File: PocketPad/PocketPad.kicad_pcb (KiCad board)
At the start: 2 copper layers, 71.6 x 60.5 mm, 35 parts, among them SW0 SW_Push, SW1 SW_Push, SW10 SW_Push, SW11 SW_Push, SW12 SW_Push, SW13 SW_Push, SW14 SW_Push, SW15 SW_Push, SW16 SW_Push, SW2 SW_Push, SW3 SW_Push, SW4 SW_Push, SW5 SW_Push, SW6 SW_Push, SW7 SW_Push, SW8 SW_Push, SW9 SW_Push

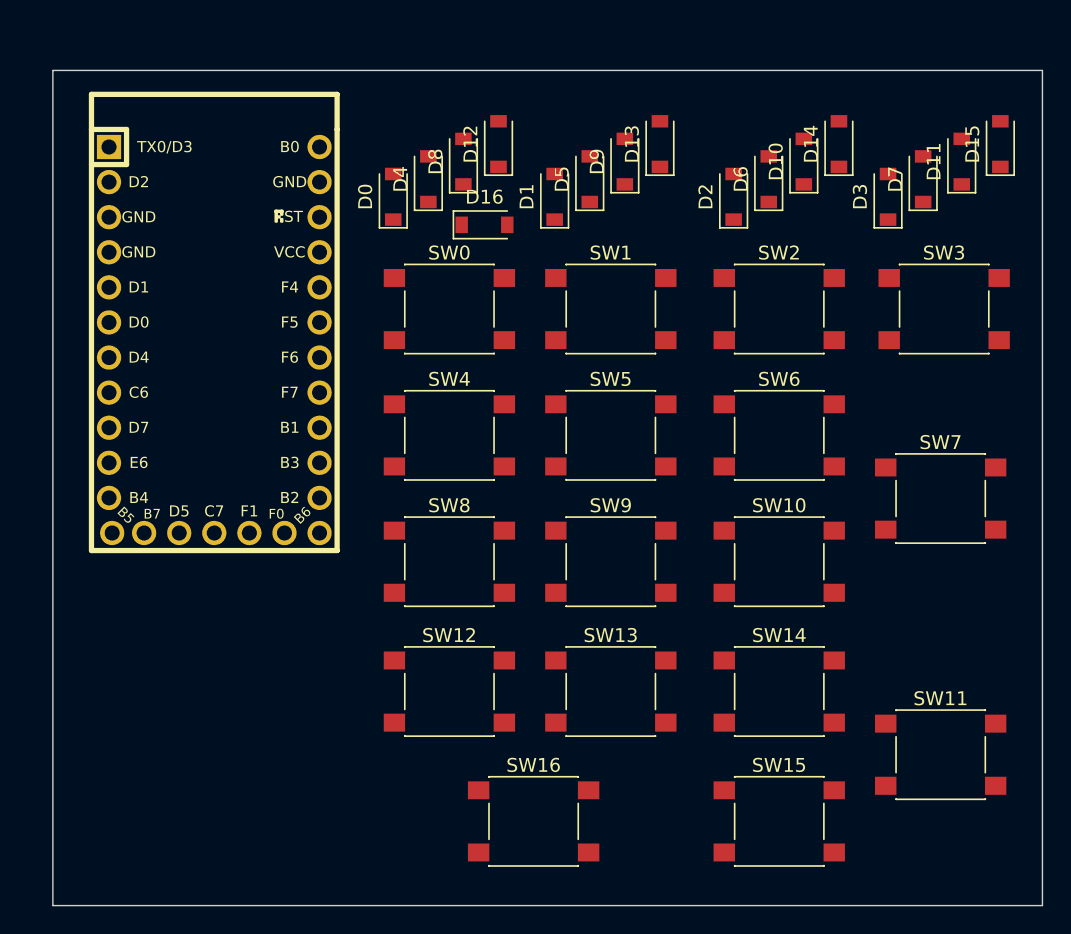
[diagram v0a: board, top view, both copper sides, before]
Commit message: Replaced Diodes. Added 3D models
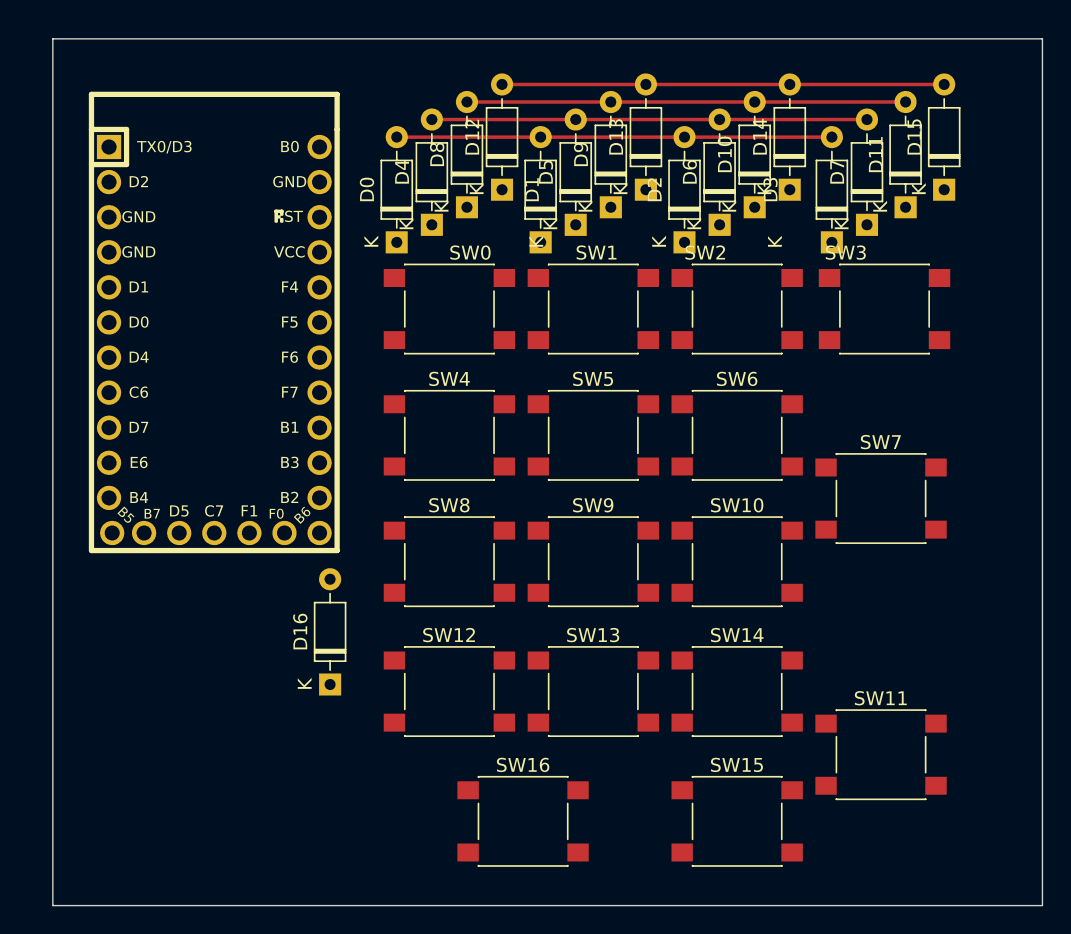
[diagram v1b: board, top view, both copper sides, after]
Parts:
- D0, D1, D10, D11, D12, D13, D14, D15, D16, D2, D3, D4, D5, D6, D7, D8, D9: footprint Diode_SMD:D_SOD-123 -> Diode_THT:D_DO-35_SOD27_P7.62mm_Horizontal
- moved D16 35.1 mm to (45.7, 82.5), turned to 90 degrees
- moved D7 5.24 mm to (84.6, 49.3)
- moved D11 5.24 mm to (87.4, 48.0)
- moved D15 5.24 mm to (90.2, 46.7)
- moved D3 5.24 mm to (82.0, 50.5)
- moved D10 4.85 mm to (76.5, 48.0)
- moved D2 4.85 mm to (71.4, 50.5)
- moved D6 4.85 mm to (73.9, 49.3)
- moved D14 4.85 mm to (79.0, 46.7)
- moved SW11 4.32 mm to (85.6, 87.6)
- moved SW3 4.32 mm to (85.9, 55.4)
- moved SW7 4.32 mm to (85.6, 69.1)
- moved D5 3.45 mm to (63.5, 49.3)
- moved D13 3.45 mm to (68.6, 46.7)
- moved D1 3.45 mm to (61.0, 50.5)
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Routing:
- net ROW3: track 0.00 -> 32.0 mm
- net ROW2: track 0.00 -> 31.8 mm
- net ROW0: track 0.00 -> 31.5 mm
- net ROW1: track 0.00 -> 31.5 mm
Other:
- board size 71.6 x 60.5 mm -> 71.6 x 62.7 mm

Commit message: V0.1 Complete
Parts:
- added D17: DIODE, Diode_THT:D_DO-35_SOD27_P7.62mm_Horizontal, F.Cu at (42.2, 82.5)
- added D18: DIODE, Diode_THT:D_DO-35_SOD27_P7.62mm_Horizontal, F.Cu at (46.5, 82.5)
- added SW17: SW_Push, Keebio:Switch_6x6x8.5, F.Cu at (44.7, 92.5)
- added SW18: SW_Push, Keebio:Switch_6x6x8.5, F.Cu at (59.9, 92.5)
- SW0, SW1, SW10, SW11, SW12, SW13, SW14, SW15, SW16, SW2, SW3, SW4, SW5, SW6, SW7, SW8, SW9: footprint Button_Switch_SMD:SW_SPST_PTS645 -> Keebio:Switch_6x6x8.5
- moved SW16 26.4 mm to (33.3, 92.5)
- moved D3 11.7 mm to (93.0, 46.2)
- moved D2 11.0 mm to (81.5, 46.2)
- moved D1 10.1 mm to (70.1, 46.2)
- moved D0 9.20 mm to (58.7, 46.2)
- moved D12 8.54 mm to (50.3, 50.0)
- moved D16 8.38 mm to (37.3, 82.5)
- moved D13 7.61 mm to (61.7, 50.0)
- moved D14 6.71 mm to (73.2, 50.0)
- moved D15 6.49 mm to (84.6, 50.0)
- moved D7 5.86 mm to (90.2, 47.5)
- moved D6 5.14 mm to (78.7, 47.5)
- moved D5 4.20 mm to (67.3, 47.5)
- moved D4 3.31 mm to (55.9, 47.5)
- moved D8 2.65 mm to (53.1, 48.8)
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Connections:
- D16 pad 2: unconnected-(D16-Pad2) -> ROW4
- MCU1 pad 16: unconnected-(MCU1-Pad16) -> ROW4
- MCU1 pad 17: unconnected-(MCU1-Pad17) -> ROW0
- MCU1 pad 18: unconnected-(MCU1-Pad18) -> ROW1
- MCU1 pad 19: unconnected-(MCU1-Pad19) -> ROW2
- MCU1 pad 20: unconnected-(MCU1-Pad20) -> ROW3
- MCU1 pad 25: unconnected-(MCU1-Pad25) -> COL0
- MCU1 pad 26: unconnected-(MCU1-Pad26) -> COL1
- MCU1 pad 27: unconnected-(MCU1-Pad27) -> COL2
- MCU1 pad 28: unconnected-(MCU1-Pad28) -> COL3
- SW0 pad 1: Net-(SW0-Pad1) -> COL0
- SW1 pad 1: Net-(SW1-Pad1) -> COL1
- SW10 pad 1: Net-(SW10-Pad1) -> COL2
- SW11 pad 1: Net-(SW11-Pad1) -> COL3
- SW12 pad 1: Net-(SW0-Pad1) -> COL0
- SW13 pad 1: Net-(SW1-Pad1) -> COL1
- SW14 pad 1: Net-(SW10-Pad1) -> COL2
- SW15 pad 1: Net-(SW11-Pad1) -> COL3
- SW16 pad 1: Net-(SW0-Pad1) -> COL0
- SW2 pad 1: Net-(SW10-Pad1) -> COL2
- SW3 pad 1: Net-(SW11-Pad1) -> COL3
- SW4 pad 1: Net-(SW0-Pad1) -> COL0
- SW5 pad 1: Net-(SW1-Pad1) -> COL1
- SW6 pad 1: Net-(SW10-Pad1) -> COL2
- SW7 pad 1: Net-(SW11-Pad1) -> COL3
- SW8 pad 1: Net-(SW0-Pad1) -> COL0
- SW9 pad 1: Net-(SW1-Pad1) -> COL1
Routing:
- net COL3: track 0.00 -> 137.9 mm
- net COL2: track 0.00 -> 118.6 mm
- net COL1: track 0.00 -> 99.5 mm
- net COL0: track 0.00 -> 68.4 mm
- net Net-(D15-Pad1): track 0.00 -> 49.0 mm
- net Net-(D11-Pad1): track 0.00 -> 38.4 mm
- net Net-(D13-Pad1): track 0.00 -> 34.8 mm
- net Net-(D12-Pad1): track 0.00 -> 34.0 mm
- net Net-(D14-Pad1): track 0.00 -> 33.8 mm
- net ROW0: track 31.5 -> 64.7 mm
- net ROW1: track 31.5 -> 58.8 mm
- net Net-(D8-Pad1): track 0.00 -> 24.7 mm
- net Net-(D9-Pad1): track 0.00 -> 24.7 mm
- net Net-(D10-Pad1): track 0.00 -> 24.6 mm
- net Net-(D18-Pad1): track 0.00 -> 23.5 mm, vias 0 -> 1
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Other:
- board outline removed

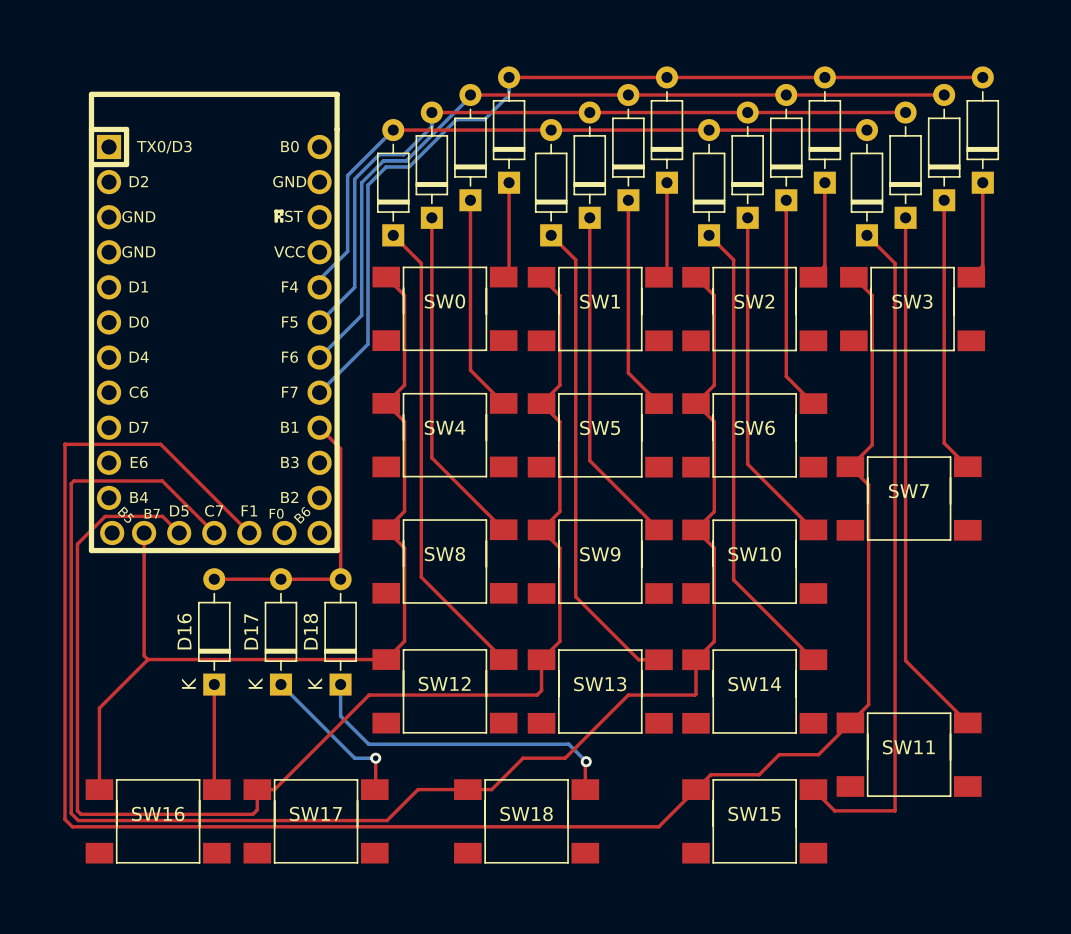
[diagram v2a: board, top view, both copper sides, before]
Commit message: Added GND plane
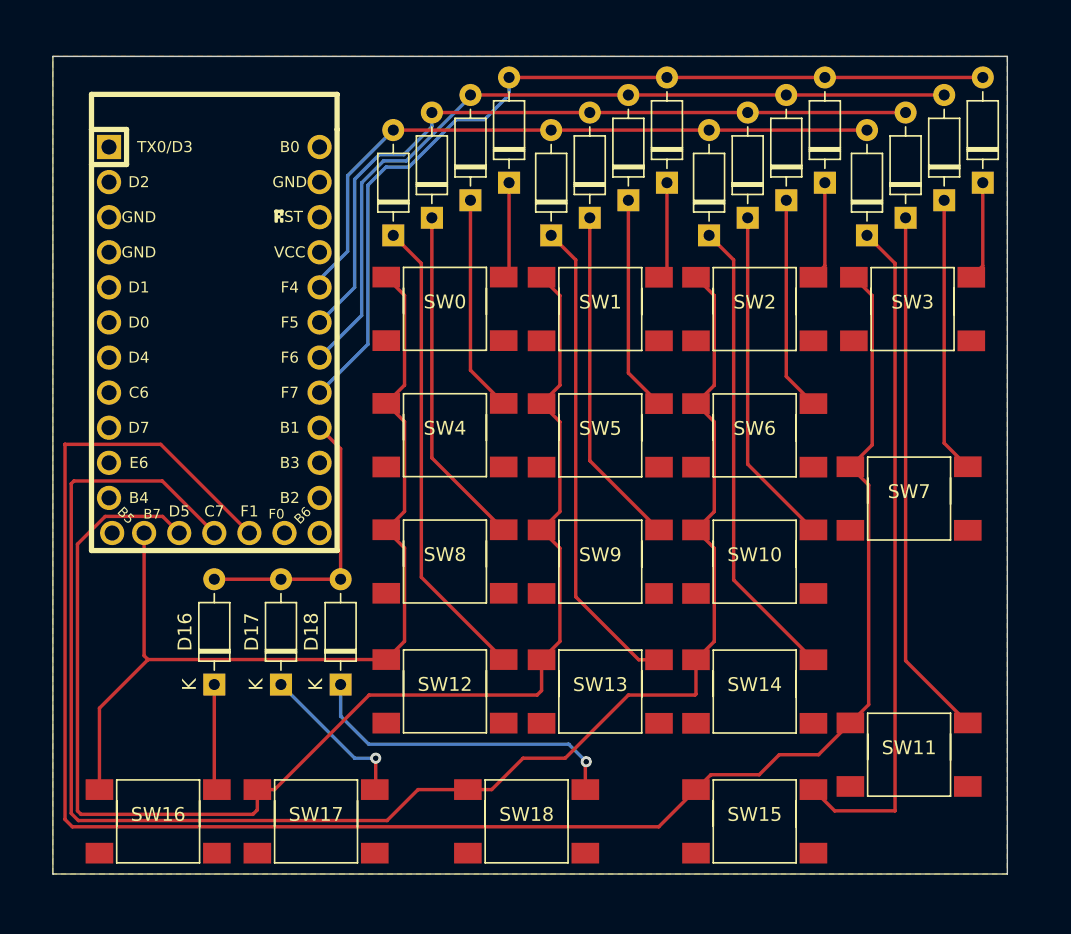
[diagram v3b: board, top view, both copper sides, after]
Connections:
- MCU1 pad 3: unconnected-(MCU1-Pad3) -> GND
- MCU1 pad 4: unconnected-(MCU1-Pad4) -> GND
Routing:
- added copper zone on F.Cu, net GND
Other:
- board outline added: 69.1 x 59.2 mm
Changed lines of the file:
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@@
   (net 1 "unconnected-(MCU1-Pad1)")
   (net 2 "unconnected-(MCU1-Pad2)")
-  (net 3 "unconnected-(MCU1-Pad3)")
-  (net 4 "unconnected-(MCU1-Pad4)")
+  (net 3 "Net-(D17-Pad1)")
+  (net 4 "GND")
   (net 5 "unconnected-(MCU1-Pad5)")
   (net 6 "unconnected-(MCU1-Pad6)")
@@
   (net 42 "ROW4")
   (net 43 "Net-(D16-Pad1)")
-  (net 44 "Net-(SW17-Pad2)")
-  (net 45 "Net-(D18-Pad1)")
-  (net 46 "unconnected-(MCU1-Pad13)")
-  (net 47 "unconnected-(MCU1-Pad14)")
-  (net 48 "unconnected-(MCU1-Pad15)")
+  (net 44 "Net-(D18-Pad1)")
+  (net 45 "unconnected-(MCU1-Pad13)")
+  (net 46 "unconnected-(MCU1-Pad14)")
+  (net 47 "unconnected-(MCU1-Pad15)")
   (footprint "Diode_THT:D_DO-35_SOD27_P7.62mm_Horizontal" (layer "F.Cu")
     (at 81.534 46.228 90)
@@
       (net 2 "unconnected-(MCU1-Pad2)") (pinfunction "RX1/PD2") (pintype "input"))
     (pad "3" thru_hole circle locked (at -8.89 7.62 270) (size 1.7526 1.7526) (drill 1.0922) (layers *.Cu *.SilkS *.Mask)
-      (net 3 "unconnected-(MCU1-Pad3)") (pinfunction "GND") (pintype "input"))
+      (net 4 "GND") (pinfunction "GND") (pintype "input"))
     (pad "4" thru_hole circle locked (at -6.35 7.62 270) (size 1.7526 1.7526) (drill 1.0922) (layers *.Cu *.SilkS *.Mask)
-      (net 4 "unconnected-(MCU1-Pad4)") (pinfunction "GND") (pintype "input"))
+      (net 4 "GND") (pinfunction "GND") (pintype "input"))
     (pad "5" thru_hole circle locked (at -3.81 7.62 270) (size 1.7526 1.7526) (drill 1.0922) (layers *.Cu *.SilkS *.Mask)
       (net 5 "unconnected-(MCU1-Pad5)") (pinfunction "2/PD1") (pintype "input"))
@@
       (net 19 "unconnected-(MCU1-Pad12)") (pinfunction "9/PB5") (pintype "input"))
     (pad "13" thru_hole circle locked (at 13.97 -7.62 270) (size 1.7526 1.7526) (drill 1.0922) (layers *.Cu *.SilkS *.Mask)
-      (net 46 "unconnected-(MCU1-Pad13)") (pinfunction "10/PB6") (pintype "input"))
+      (net 45 "unconnected-(MCU1-Pad13)") (pinfunction "10/PB6") (pintype "input"))
     (pad "14" thru_hole circle locked (at 11.43 -7.62 270) (size 1.7526 1.7526) (drill 1.0922) (layers *.Cu *.SilkS *.Mask)
-      (net 47 "unconnected-(MCU1-Pad14)") (pinfunction "16/PB2") (pintype "input"))
+      (net 46 "unconnected-(MCU1-Pad14)") (pinfunction "16/PB2") (pintype "input"))
     (pad "15" thru_hole circle locked (at 8.89 -7.62 270) (size 1.7526 1.7526) (drill 1.0922) (layers *.Cu *.SilkS *.Mask)
-      (net 48 "unconnected-(MCU1-Pad15)") (pinfunction "14/PB3") (pintype "input"))
+      (net 47 "unconnected-(MCU1-Pad15)") (pinfunction "14/PB3") (pintype "input"))
     (pad "16" thru_hole circle locked (at 6.35 -7.62 270) (size 1.7526 1.7526) (drill 1.0922) (layers *.Cu *.SilkS *.Mask)
       (net 42 "ROW4") (pinfunction "15/PB1") (pintype "input"))
@@
     (fp_line (start 2.41 -1) (end 2.41 1) (layer "F.Fab") (width 0.1))
     (pad "1" thru_hole rect (at 0 0 90) (size 1.6 1.6) (drill 0.8) (layers *.Cu *.Mask)
-      (net 45 "Net-(D18-Pad1)") (pinfunction "A") (pintype "passive"))
+      (net 44 "Net-(D18-Pad1)") (pinfunction "A") (pintype "passive"))
     (pad "2" thru_hole oval (at 7.62 0 90) (size 1.6 1.6) (drill 0.8) (layers *.Cu *.Mask)
       (net 42 "ROW4") (pinfunction "K") (pintype "passive"))
@@
       (net 14 "COL1") (pinfunction "1") (pintype "passive"))
     (pad "2" smd rect (at 4.25 -2.3 90) (size 1.5 2) (layers "F.Cu" "F.Paste" "F.Mask")
-      (net 44 "Net-(SW17-Pad2)") (pinfunction "2") (pintype "passive"))
+      (net 3 "Net-(D17-Pad1)") (pinfunction "2") (pintype "passive"))
     (pad "3" smd rect (at -4.25 2.3) (size 2 1.5) (layers "F.Cu" "F.Paste" "F.Mask"))
     (pad "4" smd rect (at 4.25 2.3) (size 2 1.5) (layers "F.Cu" "F.Paste" "F.Mask"))
@@
     (fp_line (start 0 0) (end 1.81 0) (layer "F.Fab") (width 0.1))
     (pad "1" thru_hole rect (at 0 0 90) (size 1.6 1.6) (drill 0.8) (layers *.Cu *.Mask)
-      (net 44 "Net-(SW17-Pad2)") (pinfunction "A") (pintype "passive"))
+      (net 3 "Net-(D17-Pad1)") (pinfunction "A") (pintype "passive"))
     (pad "2" thru_hole oval (at 7.62 0 90) (size 1.6 1.6) (drill 0.8) (layers *.Cu *.Mask)
       (net 42 "ROW4") (pinfunction "K") (pintype "passive"))
@@
       (net 13 "COL2") (pinfunction "1") (pintype "passive"))
     (pad "2" smd rect (at 4.25 -2.3 90) (size 1.5 2) (layers "F.Cu" "F.Paste" "F.Mask")
-      (net 45 "Net-(D18-Pad1)") (pinfunction "2") (pintype "passive"))
+      (net 44 "Net-(D18-Pad1)") (pinfunction "2") (pintype "passive"))
     (pad "3" smd rect (at -4.25 2.3) (size 2 1.5) (layers "F.Cu" "F.Paste" "F.Mask"))
     (pad "4" smd rect (at 4.25 2.3) (size 2 1.5) (layers "F.Cu" "F.Paste" "F.Mask"))
@@
     )
   )
+  (gr_rect (start 94.742 96.266) (end 25.654 37.084) (layer "Edge.Cuts") (width 0.1) (fill none))
+  (segment (start 49.022 87.884) (end 49.022 90.088) (width 0.25) (layer "F.Cu") (net 3))
+  (segment (start 49.022 90.088) (end 48.954 90.156) (width 0.25) (layer "F.Cu") (net 3))
+  (via (at 49.022 87.884) (size 0.8) (drill 0.4) (layers "F.Cu" "B.Cu") (free) (net 3))
+  (segment (start 47.498 87.884) (end 49.022 87.884) (width 0.25) (layer "B.Cu") (net 3))
+  (segment (start 42.164 82.55) (end 47.498 87.884) (width 0.25) (layer "B.Cu") (net 3))
   (segment (start 81.08 87.63) (end 83.38 85.33) (width 0.25) (layer "F.Cu") (net 12))
   (segment (start 84.959 54.397) (end 83.634 53.072) (width 0.25) (layer "F.Cu") (net 12))
@@
   (segment (start 37.338 82.55) (end 37.338 89.97) (width 0.25) (layer "F.Cu") (net 43))
   (segment (start 37.338 89.97) (end 37.524 90.156) (width 0.25) (layer "F.Cu") (net 43))
-  (segment (start 49.022 87.884) (end 49.022 90.088) (width 0.25) (layer "F.Cu") (net 44))
-  (segment (start 49.022 90.088) (end 48.954 90.156) (width 0.25) (layer "F.Cu") (net 44))
-  (via (at 49.022 87.884) (size 0.8) (drill 0.4) (layers "F.Cu" "B.Cu") (free) (net 44))
-  (segment (start 47.498 87.884) (end 49.022 87.884) (width 0.25) (layer "B.Cu") (net 44))
-  (segment (start 42.164 82.55) (end 47.498 87.884) (width 0.25) (layer "B.Cu") (net 44))
-  (segment (start 64.194 90.156) (end 64.194 88.206) (width 0.25) (layer "F.Cu") (net 45))
-  (segment (start 64.194 88.206) (end 64.262 88.138) (width 0.25) (layer "F.Cu") (net 45))
-  (via (at 64.262 88.138) (size 0.8) (drill 0.4) (layers "F.Cu" "B.Cu") (free) (net 45))
-  (segment (start 46.482 84.836) (end 48.514 86.868) (width 0.25) (layer "B.Cu") (net 45))
-  (segment (start 48.514 86.868) (end 62.992 86.868) (width 0.25) (layer "B.Cu") (net 45))
-  (segment (start 62.992 86.868) (end 64.262 88.138) (width 0.25) (layer "B.Cu") (net 45))
-  (segment (start 46.482 82.55) (end 46.482 84.836) (width 0.25) (layer "B.Cu") (net 45))
+  (segment (start 64.194 90.156) (end 64.194 88.206) (width 0.25) (layer "F.Cu") (net 44))
+  (segment (start 64.194 88.206) (end 64.262 88.138) (width 0.25) (layer "F.Cu") (net 44))
+  (via (at 64.262 88.138) (size 0.8) (drill 0.4) (layers "F.Cu" "B.Cu") (free) (net 44))
+  (segment (start 46.482 84.836) (end 48.514 86.868) (width 0.25) (layer "B.Cu") (net 44))
+  (segment (start 48.514 86.868) (end 62.992 86.868) (width 0.25) (layer "B.Cu") (net 44))
+  (segment (start 62.992 86.868) (end 64.262 88.138) (width 0.25) (layer "B.Cu") (net 44))
+  (segment (start 46.482 82.55) (end 46.482 84.836) (width 0.25) (layer "B.Cu") (net 44))
+  (zone (net 4) (net_name "GND") (layer "F.Cu") (hatch edge 0.508)
+    (connect_pads (clearance 0.508))
+    (min_thickness 0.254)
+    (fill (thermal_gap 0.508) (thermal_bridge_width 0.508))
+    (polygon
+      (pts
+        (xy 94.742 96.266)
+        (xy 25.654 96.266)
+        (xy 25.654 37.084)
+        (xy 94.742 37.084)
+      )
+    )
+  )
 )

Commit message: Added edgecut with mounting holes
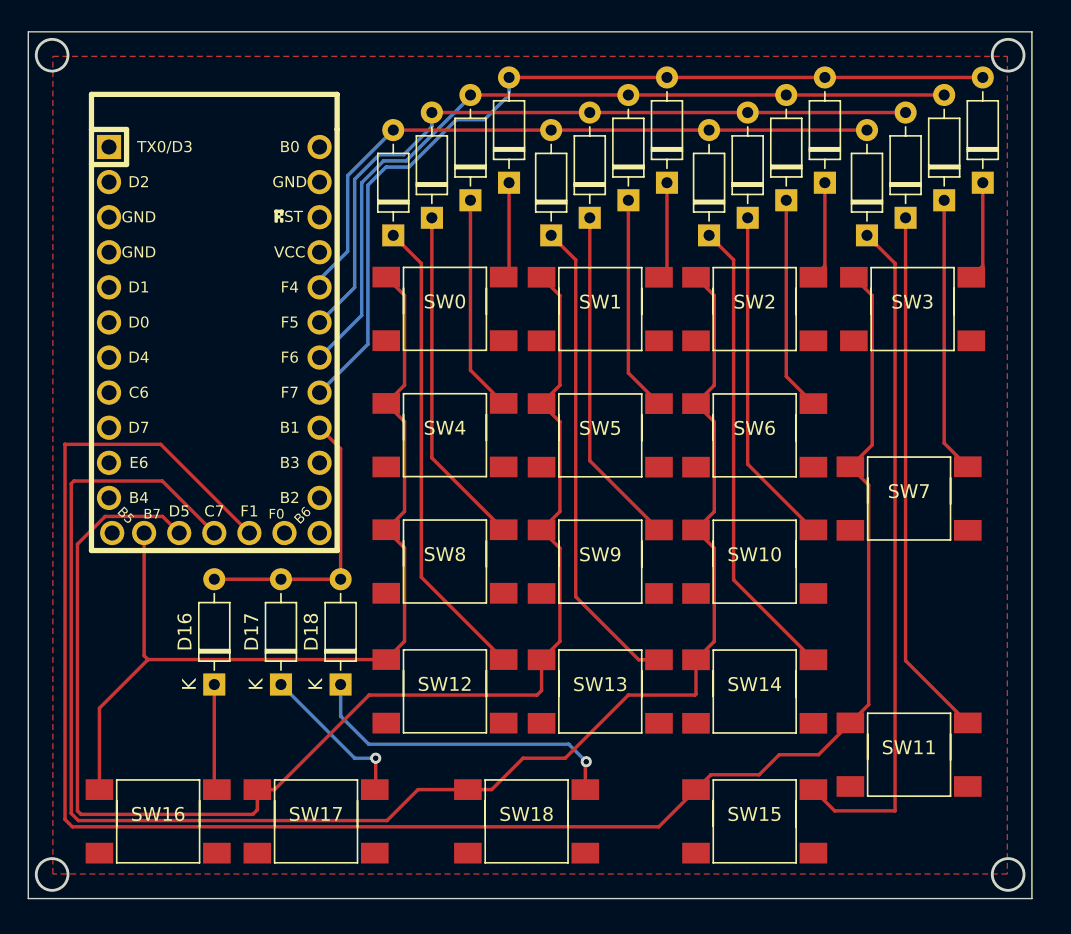
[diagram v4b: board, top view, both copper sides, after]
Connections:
- MCU1 pad 23: unconnected-(MCU1-Pad23) -> GND
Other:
- board size 69.1 x 59.2 mm -> 72.6 x 62.7 mm
